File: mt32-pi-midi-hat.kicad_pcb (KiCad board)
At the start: 2 copper layers, 64.3 x 56 mm, 14 parts, among them J1 MIDI IN, J2 OLED, J3 OLED, J4 DAC BOARD, J5 DAC BOARD, J6 Hitachi HD44780, J7 POST, J8 POST, U1 H11L1

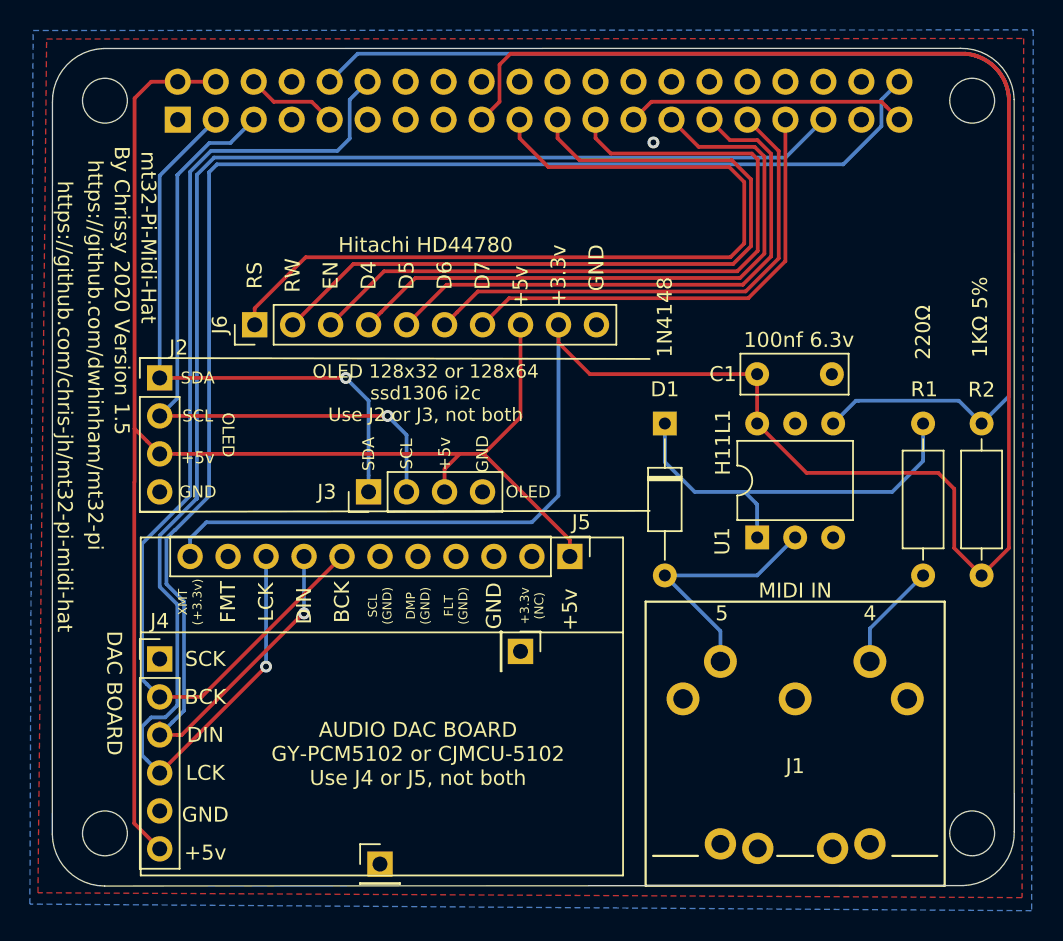
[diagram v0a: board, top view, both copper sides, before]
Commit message: Version 1.6
1. Removed Hitachi 4bit version
2. Added new buttons from version 0.8 of the mt32-pi project
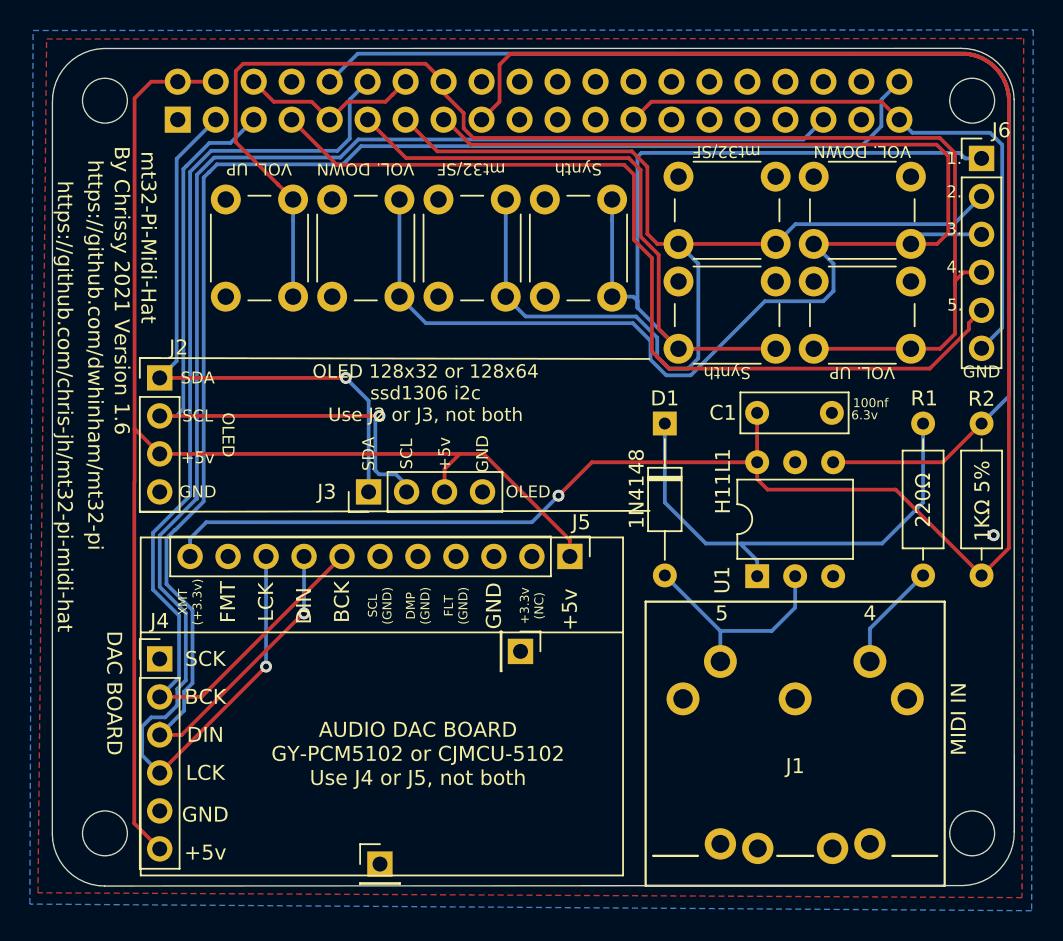
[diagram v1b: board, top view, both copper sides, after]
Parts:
- added SW1: BUTTON_1, Button_Switch_THT:SW_PUSH_6mm_SLIM, F.Cu at (140.6, 91.3)
- added SW2: BUTTON_2, Button_Switch_THT:SW_PUSH_6mm_SLIM, F.Cu at (140.6, 84.3)
- added SW3: BUTTON_3, Button_Switch_THT:SW_PUSH_6mm_SLIM, F.Cu at (149.7, 84.3)
- added SW4: BUTTON_4, Button_Switch_THT:SW_PUSH_6mm_SLIM, F.Cu at (149.7, 91.3)
- added SW5: BUTTON_1, Button_Switch_THT:SW_PUSH_6mm_SLIM, F.Cu at (131.7, 92.4)
- added SW6: BUTTON_2, Button_Switch_THT:SW_PUSH_6mm_SLIM, F.Cu at (124.6, 92.4)
- added SW7: BUTTON_3, Button_Switch_THT:SW_PUSH_6mm_SLIM, F.Cu at (117.4, 92.4)
- added SW8: BUTTON_4, Button_Switch_THT:SW_PUSH_6mm_SLIM, F.Cu at (110.3, 92.4)
- C1: value 100nf 6.3v -> 100nf
- J6: value Hitachi HD44780 -> CONTROL_PINS; footprint Connector_PinHeader_2.54mm:PinHeader_1x10_P2.54mm_Vertical -> Connector_PinHeader_2.54mm:PinHeader_1x06_P2.54mm_Vertical
- moved J6 49.9 mm to (160.9, 83.1), turned to 0 degrees
- moved C1 2.59 mm to (145.9, 100.1)
- moved U1 2.59 mm to (145.9, 111.0)
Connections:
- J1 pad 1: Net-(J1-Pad1) -> (no net)
- J1 pad 2: Net-(J1-Pad2) -> (no net)
- J1 pad 3: Net-(J1-Pad3) -> (no net)
- J5 pad 2: Net-(J5-Pad2) -> (no net)
- J6 pad 1: RS -> BUTTON_1
- J6 pad 2: RW -> BUTTON_2
- J6 pad 3: EN -> BUTTON_3
- J6 pad 4: D4 -> BUTTON_4
- J6 pad 5: D5 -> BUTTON_5
- J6 pad 6: D6 -> GND
- J7 pad 1: Net-(J7-Pad1) -> (no net)
- J8 pad 1: Net-(J8-Pad1) -> (no net)
- Pi1 pad 1: Net-(Pi1-Pad1) -> (no net)
- Pi1 pad 11: Net-(Pi1-Pad11) -> BUTTON_1
- Pi1 pad 13: Net-(Pi1-Pad13) -> BUTTON_2
- Pi1 pad 15: Net-(Pi1-Pad15) -> BUTTON_3
- Pi1 pad 16: Net-(Pi1-Pad16) -> BUTTON_4
- Pi1 pad 18: Net-(Pi1-Pad18) -> (no net)
- Pi1 pad 19: RS -> (no net)
- Pi1 pad 20: Net-(Pi1-Pad20) -> (no net)
- Pi1 pad 21: RW -> (no net)
- Pi1 pad 22: Net-(Pi1-Pad22) -> (no net)
- Pi1 pad 23: EN -> (no net)
- Pi1 pad 24: Net-(Pi1-Pad24) -> (no net)
- Pi1 pad 26: Net-(Pi1-Pad26) -> (no net)
- Pi1 pad 27: D4 -> (no net)
- Pi1 pad 28: Net-(Pi1-Pad28) -> (no net)
- Pi1 pad 29: D5 -> (no net)
- Pi1 pad 30: Net-(Pi1-Pad30) -> (no net)
- Pi1 pad 31: D6 -> (no net)
- Pi1 pad 32: Net-(Pi1-Pad32) -> (no net)
- Pi1 pad 33: D7 -> (no net)
- Pi1 pad 34: Net-(Pi1-Pad34) -> (no net)
- Pi1 pad 36: Net-(Pi1-Pad36) -> (no net)
- Pi1 pad 37: Net-(Pi1-Pad37) -> (no net)
- Pi1 pad 38: Net-(Pi1-Pad38) -> (no net)
- Pi1 pad 7: Net-(Pi1-Pad7) -> BUTTON_5
- Pi1 pad 8: Net-(Pi1-Pad8) -> (no net)
- U1 pad 3: Net-(U1-Pad3) -> (no net)
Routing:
- net BUTTON_3: track 0.00 -> 98.7 mm
- net BUTTON_4: track 0.00 -> 92.7 mm
- net BUTTON_1: track 0.00 -> 85.2 mm
- net BUTTON_2: track 0.00 -> 76.5 mm
- net BUTTON_5: track 0.00 -> 61.3 mm
- net RS: track 57.2 -> 0.00 mm
- net RW: track 52.6 -> 0.00 mm
- net EN: track 49.4 -> 0.00 mm
- net D4: track 42.2 -> 0.00 mm
- net D5: track 38.2 -> 0.00 mm
- net D6: track 34.3 -> 0.00 mm
- net D7: track 31.5 -> 0.00 mm
- net GND: track 24.9 -> 52.8 mm
- net +3V3: track 151.5 -> 136.2 mm, vias 0 -> 1
- net +5V: track 102.7 -> 93.0 mm
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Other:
- board text added: "1."
- board text added: "2."
- board text added: "3."
- board text added: "4."
- board text added: "5."
- board text added: "6.3v"
- board text added: "By Chrissy 2021 Version 1.6"
- board text added: "Synth"
- board text added: "VOL. DOWN"
- board text added: "VOL. UP"
- board text added: "mt32/SF"
- board text removed: "+3.3v"
- board text removed: "D4"
- board text removed: "D5"
- board text removed: "D6"
- board text removed: "D7"
- board text removed: "EN"
- board text removed: "RS"
- board text removed: "RW"

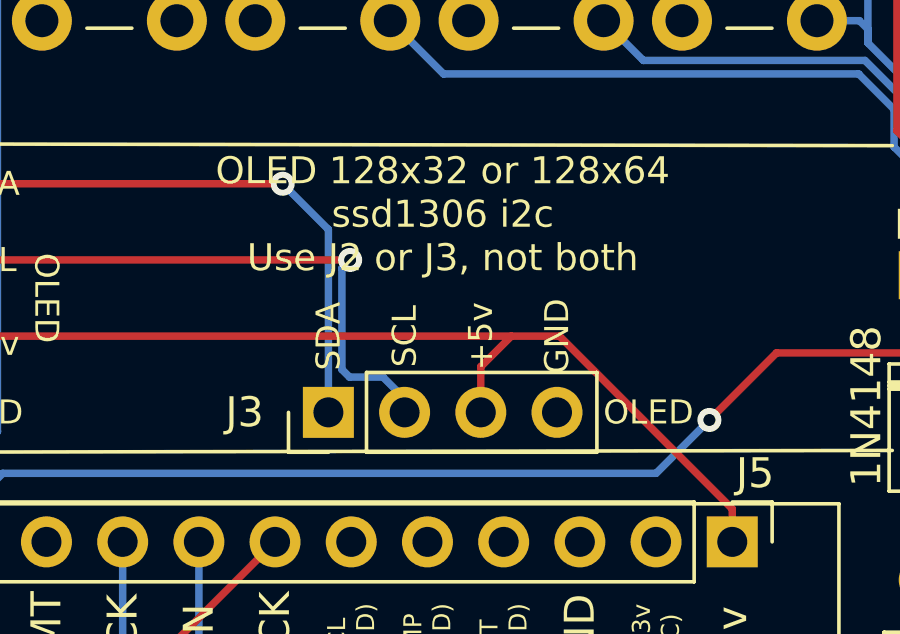
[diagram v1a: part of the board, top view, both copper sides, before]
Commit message: fix wrong date on back
fixed wrong version and date on back of pcb
slight adjustment of 128x64 oled pins
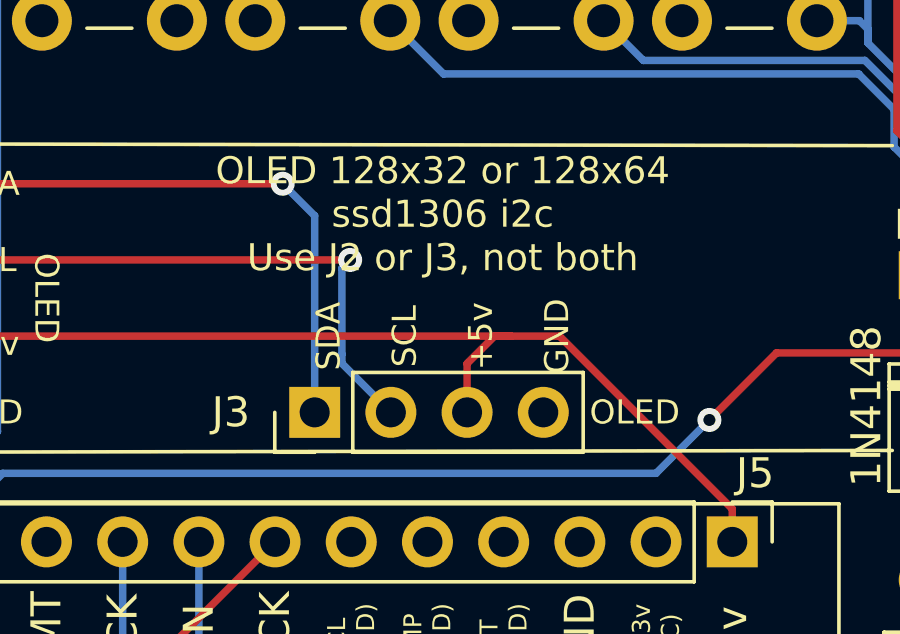
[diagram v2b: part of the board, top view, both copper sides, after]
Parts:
- moved J3 0.46 mm to (119.4, 105.4)
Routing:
- net +5V: track 93.0 -> 93.5 mm
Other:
- board text removed: "By Chrissy 2020 Version 1.5"
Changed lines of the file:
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@@
   )
   (module Connector_PinHeader_2.54mm:PinHeader_1x04_P2.54mm_Vertical (layer F.Cu)
-    (at 119.888 105.41 90)
+    (at 119.4308 105.41 90)
     (descr "Through hole straight pin header, 1x04, 2.54mm pitch, single row")
     (tags "Through hole pin header THT 1x04 2.54mm single row")
@@
     (effects (font (size 1 1) (thickness 0.15)) (justify mirror))
   )
-  (gr_text "By Chrissy 2020 Version 1.5" (at 137.922 86.36) (layer B.SilkS)
+  (gr_text "By Chrissy 2021 Version 1.6" (at 137.922 86.36) (layer B.SilkS)
     (effects (font (size 1 1) (thickness 0.15)) (justify mirror))
   )
@@
   (segment (start 125.984 102.87) (end 105.918 102.87) (width 0.25) (layer F.Cu) (net 4) (status 20))
   (segment (start 133.35 109.728) (end 133.35 108.628) (width 0.25) (layer F.Cu) (net 4) (status 10))
-  (segment (start 124.968 103.886) (end 125.984 102.87) (width 0.25) (layer F.Cu) (net 4))
-  (segment (start 124.968 105.41) (end 124.968 103.886) (width 0.25) (layer F.Cu) (net 4) (status 10))
   (segment (start 127.592 102.87) (end 125.984 102.87) (width 0.25) (layer F.Cu) (net 4))
+  (segment (start 125.984 102.87) (end 125.4252 102.87) (width 0.25) (layer F.Cu) (net 4))
+  (segment (start 124.5108 103.7844) (end 124.5108 105.41) (width 0.25) (layer F.Cu) (net 4))
+  (segment (start 125.4252 102.87) (end 124.5108 103.7844) (width 0.25) (layer F.Cu) (net 4))
   (segment (start 110.648045 82.074455) (end 109.244174 82.074455) (width 0.25) (layer B.Cu) (net 5))
   (segment (start 112.2045 80.518) (end 110.648045 82.074455) (width 0.25) (layer B.Cu) (net 5) (status 10))
@@
   (segment (start 107.49999 99.86561) (end 107.0356 100.33) (width 0.25) (layer B.Cu) (net 5))
   (segment (start 107.698914 83.619714) (end 107.49999 83.818639) (width 0.25) (layer B.Cu) (net 5))
-  (segment (start 120.33801 103.98041) (end 120.33801 100.60499) (width 0.25) (layer B.Cu) (net 5))
-  (segment (start 121.710199 104.234999) (end 120.592599 104.234999) (width 0.25) (layer B.Cu) (net 5))
-  (segment (start 120.592599 104.234999) (end 120.33801 103.98041) (width 0.25) (layer B.Cu) (net 5))
-  (segment (start 122.428 104.9528) (end 121.710199 104.234999) (width 0.25) (layer B.Cu) (net 5) (status 10))
   (segment (start 122.428 105.41) (end 122.428 104.9528) (width 0.25) (layer B.Cu) (net 5) (status 30))
   (segment (start 120.33801 100.60499) (end 120.613 100.33) (width 0.25) (layer B.Cu) (net 5))
   (via (at 120.613 100.33) (size 0.8) (drill 0.4) (layers F.Cu B.Cu) (net 5))
   (segment (start 120.613 100.33) (end 105.918 100.33) (width 0.25) (layer F.Cu) (net 5) (status 20))
-  (segment (start 119.888 105.41) (end 119.888 99.314) (width 0.25) (layer B.Cu) (net 6) (status 10))
+  (segment (start 120.33801 103.77721) (end 120.33801 103.47241) (width 0.25) (layer B.Cu) (net 5))
+  (segment (start 121.9708 105.41) (end 120.33801 103.77721) (width 0.25) (layer B.Cu) (net 5))
+  (segment (start 120.33801 103.47241) (end 120.33801 100.60499) (width 0.25) (layer B.Cu) (net 5))
   (via (at 118.364 97.79) (size 0.8) (drill 0.4) (layers F.Cu B.Cu) (net 6))
-  (segment (start 119.888 99.314) (end 118.364 97.79) (width 0.25) (layer B.Cu) (net 6))
   (segment (start 118.364 97.79) (end 105.918 97.79) (width 0.25) (layer F.Cu) (net 6) (status 20))
   (segment (start 107.04998 96.65802) (end 107.04998 83.13252) (width 0.25) (layer B.Cu) (net 6))
   (segment (start 107.04998 83.13252) (end 109.6645 80.518) (width 0.25) (layer B.Cu) (net 6) (status 20))
   (segment (start 105.918 97.79) (end 107.04998 96.65802) (width 0.25) (layer B.Cu) (net 6) (status 10))
+  (segment (start 118.364 97.79) (end 119.4308 98.8568) (width 0.25) (layer B.Cu) (net 6))
+  (segment (start 119.4308 98.8568) (end 119.4308 105.41) (width 0.25) (layer B.Cu) (net 6))
   (segment (start 117.2845 77.978) (end 119.157465 76.105035) (width 0.25) (layer B.Cu) (net 7) (status 10))
   (segment (start 162.085186 77.372082) (end 162.148178 77.459621) (width 0.25) (layer B.Cu) (net 7))

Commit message: Version 1.7
Fixed Silk Screen error for buttons mt32/SF and Synth
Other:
- board text added: "By Chrissy 2021 Version 1.7"
- board text removed: "By Chrissy 2021 Version 1.6"

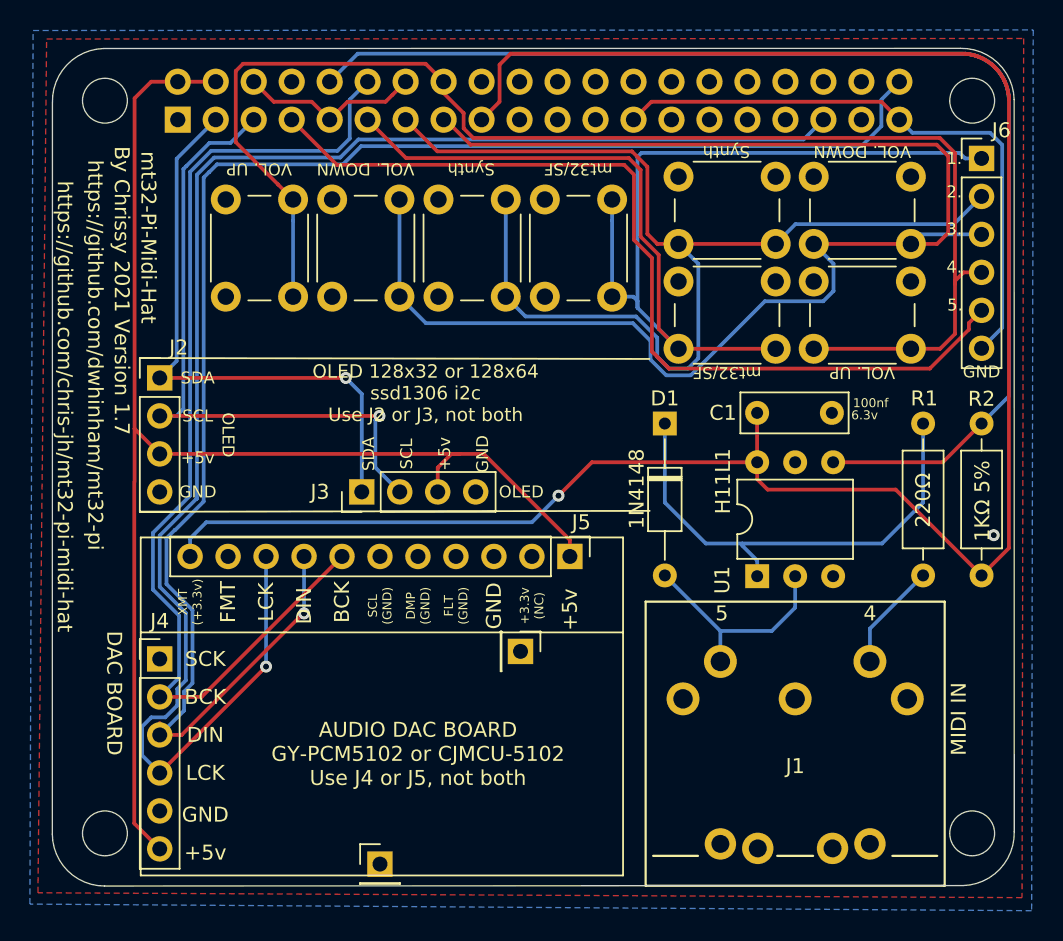
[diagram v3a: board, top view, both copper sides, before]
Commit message: V1.7.1
Moved the Midi Din Slightly, may have caused issues with OSHPark.
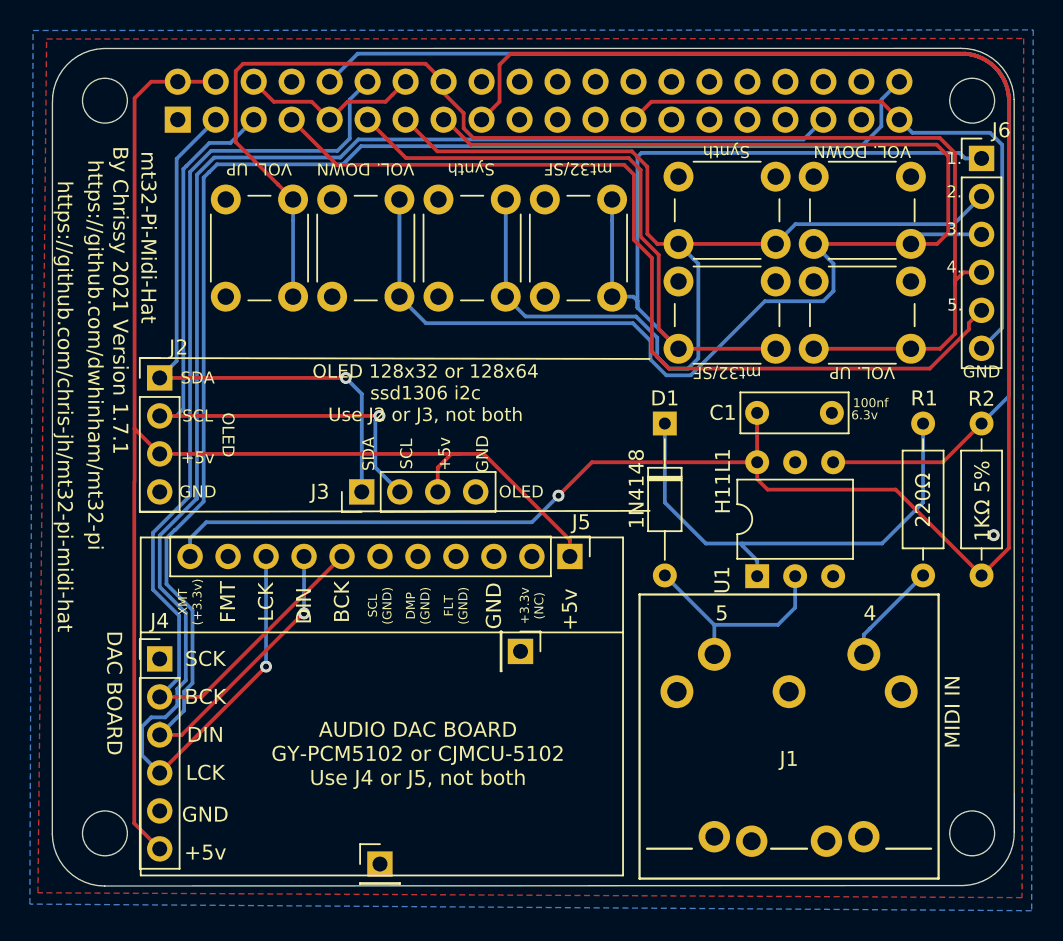
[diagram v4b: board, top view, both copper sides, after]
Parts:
- moved J1 0.63 mm to (148.0, 118.8)
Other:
- rule pad_to_mask_clearance: 0.051 -> 0
- board text added: "By Chrissy 2021 Version 1.7.1"
- board text removed: "By Chrissy 2021 Version 1.7"
